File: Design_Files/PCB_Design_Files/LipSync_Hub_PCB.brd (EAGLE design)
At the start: 80 x 64.9 mm, 30 parts, among them J1 5555165-1, J2 HEADER_MALE-1X04, J3 HEADER_FEMALE-1X290, SW1 CUI_SJ1-3535NGSJ1-3535NG, SW2 CUI_SJ1-3535NGSJ1-3535NG, SW3 CUI_SJ1-3535NGSJ1-3535NG, U1 SEEEDSTUDIO_XIAOXIAO-NRF52840

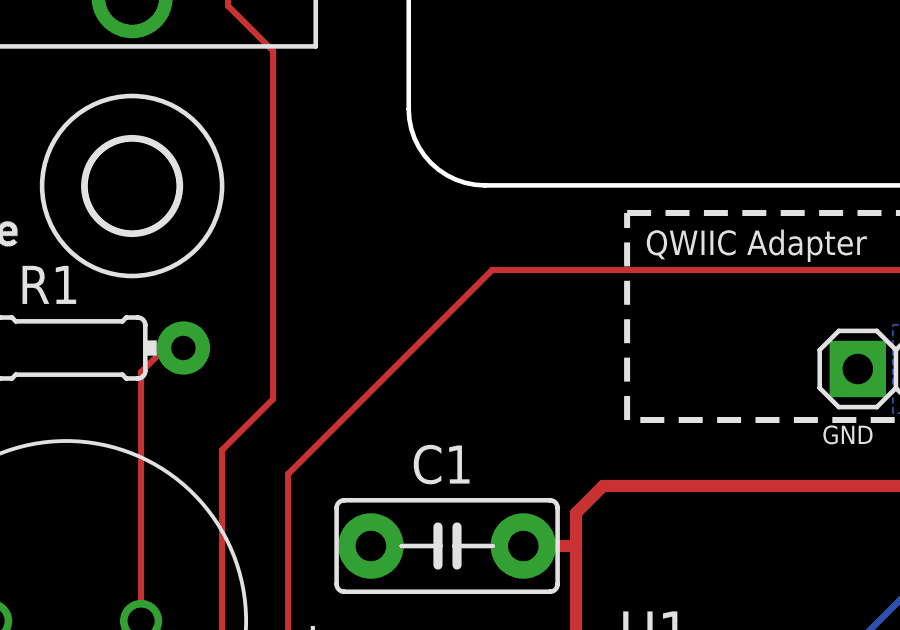
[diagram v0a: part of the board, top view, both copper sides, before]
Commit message: Add Open Source Hardware Certification
Add Open Source Hardware information to readme and PCB
Add license graphic
Update PCB Build Files
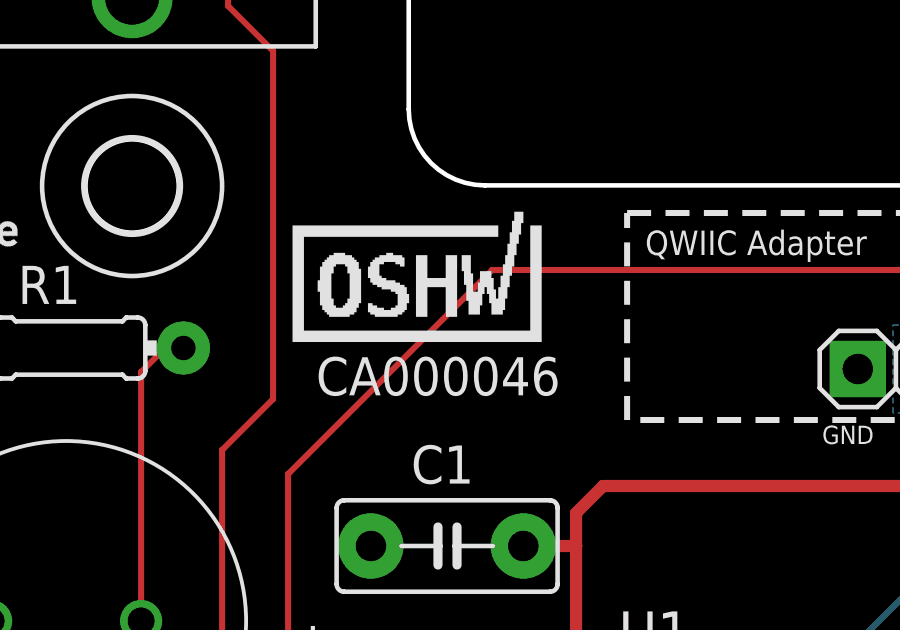
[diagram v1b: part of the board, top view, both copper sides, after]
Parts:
- added U$4: CA000046, OSHWA:CERT-SMALL-SILK
- U$2: value CA######## -> CA000046
- moved U$2 90.2 mm to (-16.8, -8.00)
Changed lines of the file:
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@@
 </element>
 <element name="U$1" library="MMC Eagle" library_urn="urn:adsk.eagle:library:13126479" package="OSHW_SMALL_LOGO" package3d_urn="urn:adsk.eagle:package:38381648/1" value="" x="-35.6" y="-2" smashed="yes"/>
-<element name="U$2" library="OSHWA" package="CERT-SMALL-SILK" value="CA########" x="70.3" y="15.5" smashed="yes" rot="MR0">
-<attribute name="VALUE" x="73.66994375" y="13.722" size="1.27" layer="22" font="vector" ratio="12" rot="MR0"/>
+<element name="U$2" library="OSHWA" package="CERT-SMALL-SILK" value="CA000046" x="-16.8" y="-8" smashed="yes" rot="MR0">
+<attribute name="VALUE" x="-13.43005625" y="-9.778" size="1.27" layer="22" font="vector" ratio="12" rot="MR0"/>
 </element>
 <element name="U$3" library="MMC Eagle" library_urn="urn:adsk.eagle:library:13126479" package="LABEL-LIPSYNC-X-LG" package3d_urn="urn:adsk.eagle:package:42121751/1" value="" x="24.1" y="-8.1" smashed="yes"/>
+<element name="U$4" library="OSHWA" package="CERT-SMALL-SILK" value="CA000046" x="-18.5" y="-8" smashed="yes">
+<attribute name="VALUE" x="-21.86994375" y="-9.778" size="1.27" layer="21" font="vector" ratio="12"/>
+</element>
 </elements>
 <signals>
